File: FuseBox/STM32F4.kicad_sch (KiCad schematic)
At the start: 25 parts, among them J1 61301611121, J2 61301611121, J3 61301611121, J4 61301611121, J5 61301611121, U1 STM32F407VGTx

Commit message: some foo
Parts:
- added C4: 10p, symbol Device:C
- added X1: CG048748M, Custom:CG048748M, symbol Custom:CG048748M
- renumbered C1 to C?, C8 to C?, C9 to C?, C15 to C?, C2 to C?, C11 to C?, C12 to C?, C6 to C?, C14 to C?, C10 to C?, C3 to C?, C5 to C?, C13 to C?, C4 to C?, C7 to C?, FB1 to FB?, J4 to J?, J2 to J?, J3 to J?, J1 to J?, J5 to J?, R1 to R?, R2 to R?, R3 to R?, U1 to U3
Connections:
- net GND: now also C?.2, R?.1, C4.1; no longer R?.2
- net at U3.12 (PH0): now also C?.2, X1.1
- net at U3.13 (PH1): now also C4.2, X1.2
- net at R?.2, U3.14 (NRST): now also C?.1; no longer C?.2
- net at U3.94 (BOOT0): now also R?.2; no longer R?.1
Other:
- moved on the sheet: C15, C?, FB?, J?, R?, U3

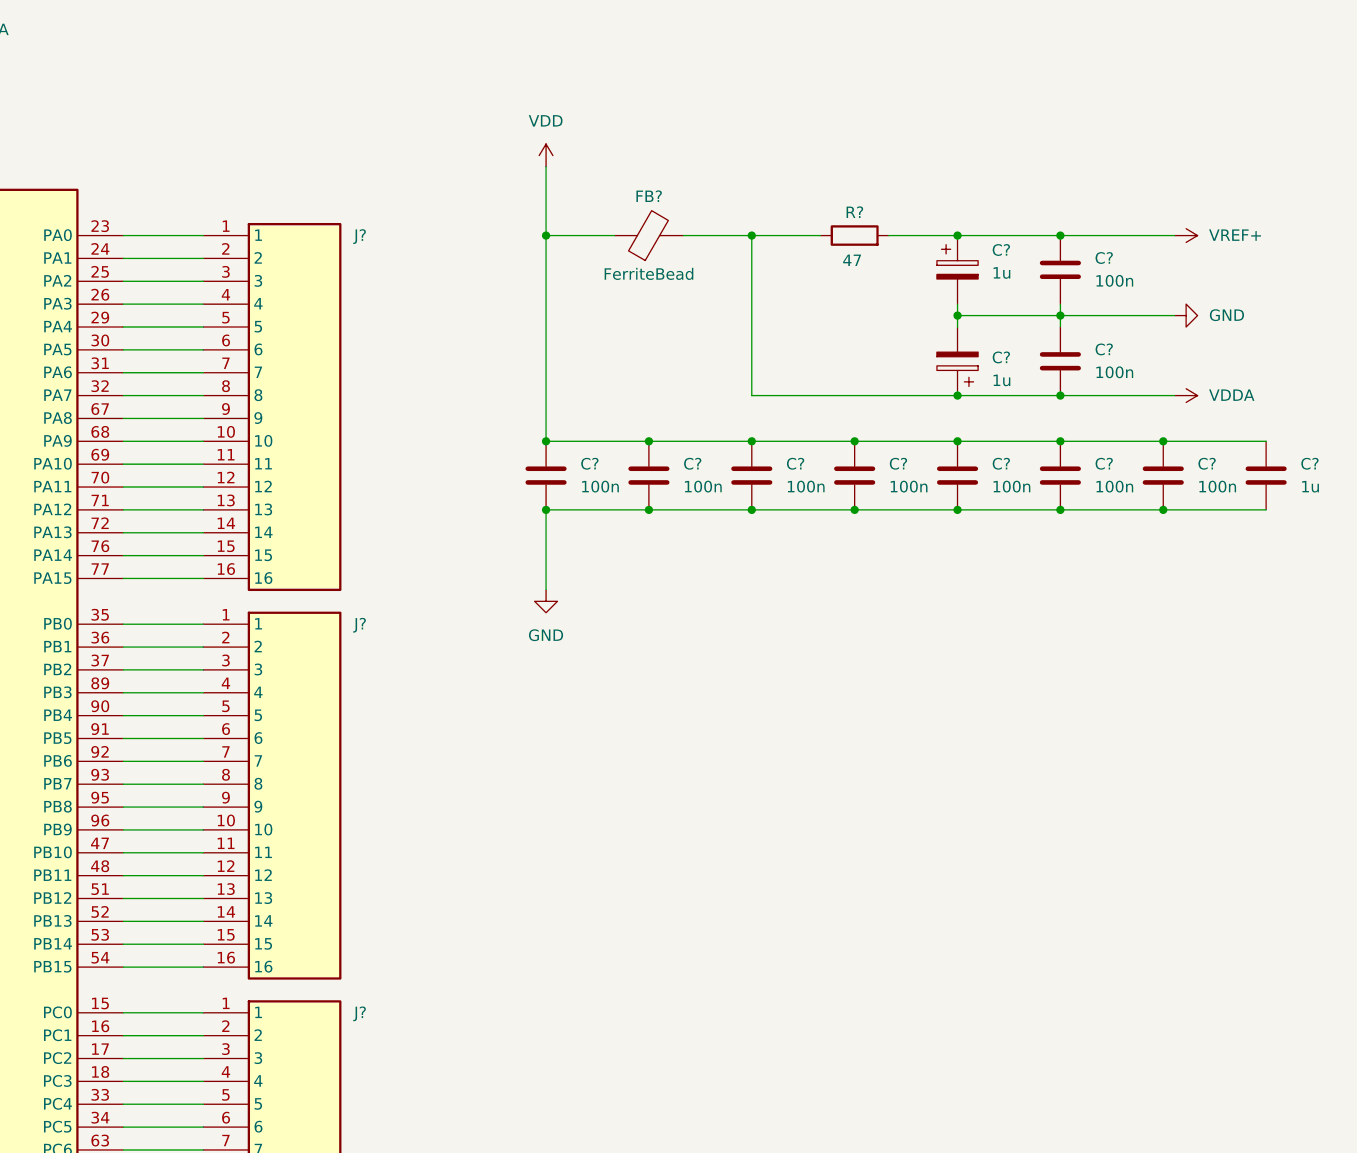
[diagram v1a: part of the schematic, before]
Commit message: added ICE40HX
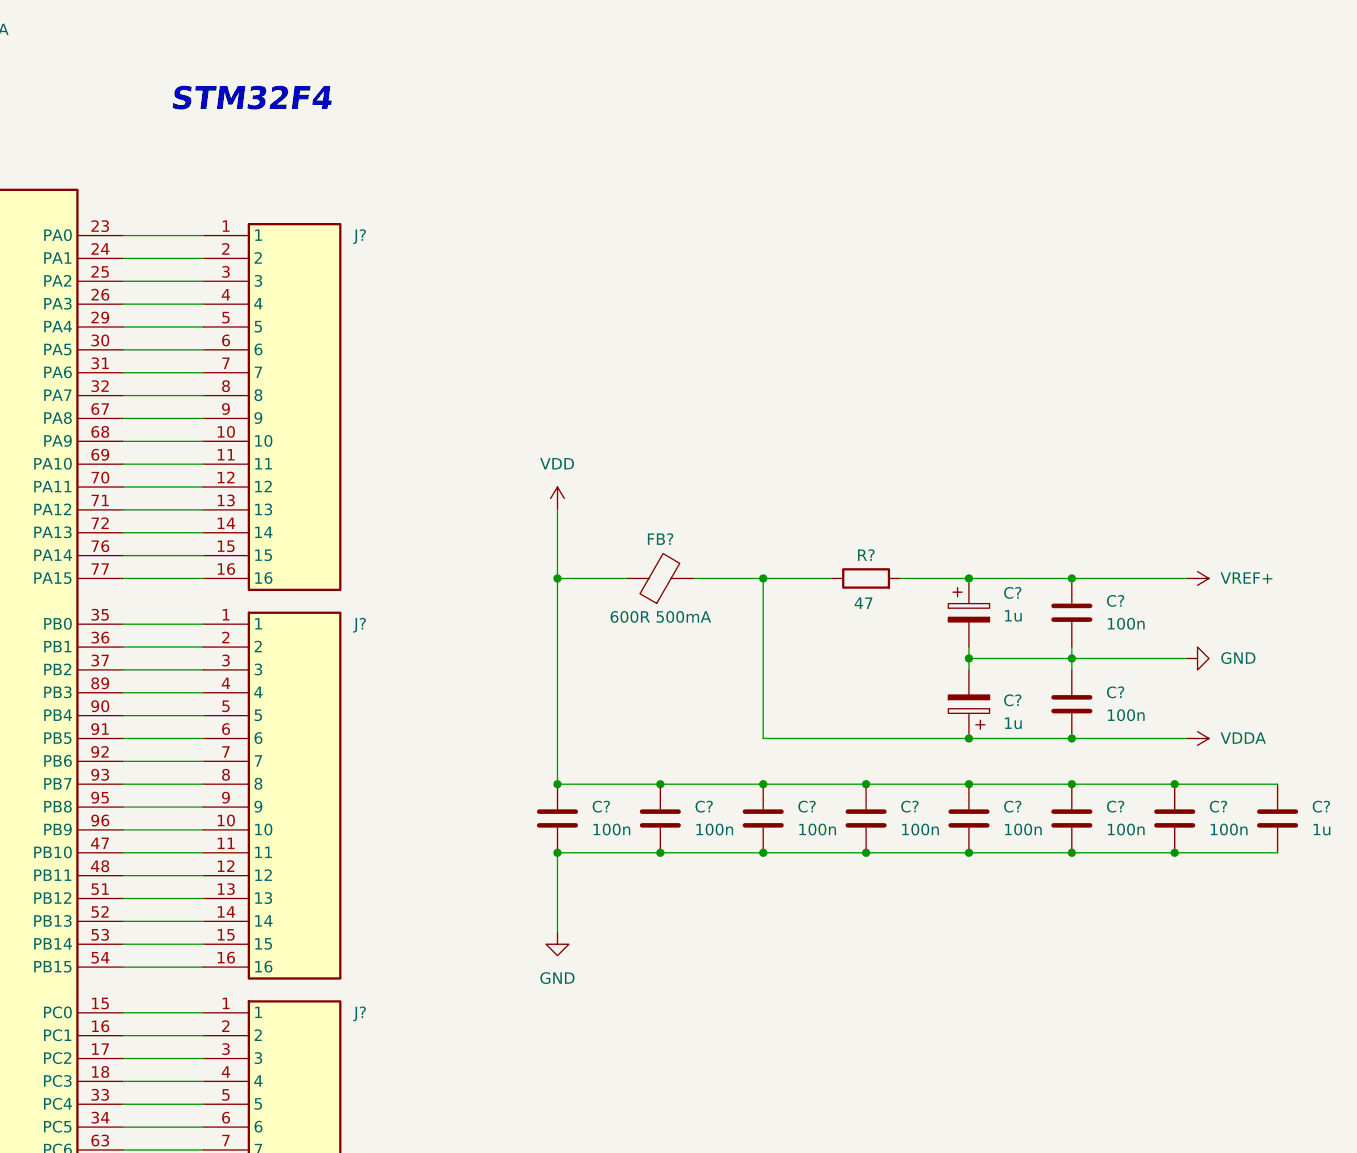
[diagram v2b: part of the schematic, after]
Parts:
- added C?: 100n, symbol Device:C
- C15: renamed from C?; value 100n -> 10p
- FB?: value FerriteBead -> 600R 500mA
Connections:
- net GND: now also C?.2; no longer C15.2
- net at R?.2, U3.14 (NRST): now also C?.1; no longer C15.1
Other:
- note added: "STM32F4"
- moved on the sheet: C?, FB?, R?

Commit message: changes
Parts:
- removed X1: CG048748M, Custom:CG048748M, symbol Custom:CG048748M
- added X1: STDCSU18M, Custom:STDCSU18M, symbol Custom:STDCSU18M
- C15, C4: value 10p -> 20p
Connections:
- net at C15.2, U3.12 (PH0): now also X1.1
- net at C4.2, U3.13 (PH1): now also X1.2
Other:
- note removed: "STM32F4"
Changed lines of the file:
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@@
 	(generator_version "9.0")
 	(paper "A4")
-	(text "STM32F4"
-		(exclude_from_sim no)
-		(at 150.114 26.924 0)
-		(effects
-			(font
-				(size 2.54 2.54)
-				(thickness 0.508)
-				(bold yes)
-				(italic yes)
-			)
-		)
-	)
 	(junction
 		(at 184.15 110.49)
@@
 	)
 	(symbol
-		(lib_id "Custom:CG048748M")
-		(at 30.48 69.85 0)
-		(unit 1)
-		(exclude_from_sim no)
-		(in_bom yes)
-		(on_board yes)
-		(dnp no)
-		(property "Reference" "X1"
-			(at 35.56 65.532 0)
-			(effects
-				(font
-					(size 1.524 1.524)
-				)
-			)
-		)
-		(property "Value" "CG048748M"
-			(at 35.306 74.93 0)
-			(effects
-				(font
-					(size 1.524 1.524)
-				)
-			)
-		)
-		(property "Footprint" "Custom:CG048748M"
-			(at 34.798 78.486 0)
-			(effects
-				(font
-					(size 1.27 1.27)
-					(italic yes)
-				)
-				(hide yes)
-			)
-		)
-		(property "Datasheet" "CG04874-8M"
-			(at 35.052 76.454 0)
-			(effects
-				(font
-					(size 1.27 1.27)
-					(italic yes)
-				)
-				(hide yes)
-			)
-		)
-		(property "Description" ""
-			(at 30.48 69.85 0)
-			(effects
-				(font
-					(size 1.27 1.27)
-				)
-				(hide yes)
-			)
-		)
-		(pin "1"
-		)
-		(pin "2"
-		)
-		(instances
-			(project ""
-				(path "/7cec0856-4a31-46c4-b6e3-cba19fcff38c/e599326e-505d-4a4a-8448-d1c391dfbddc"
-					(reference "X1")
-					(unit 1)
-				)
-			)
-		)
-	)
-	(symbol
 		(lib_id "power:GND")
 		(at 184.15 119.38 0)
@@
 			)
 		)
-		(property "Value" "10p"
+		(property "Value" "20p"
 			(at 29.21 83.8199 0)
 			(effects
@@
 			)
 		)
-		(property "Value" "10p"
+		(property "Value" "20p"
 			(at 49.53 83.8199 0)
 			(effects
@@
 					(unit 1)
 				)
+			)
+		)
+	)
+	(symbol
+		(lib_id "Custom:STDCSU18M")
+		(at 30.48 69.85 0)
+		(unit 1)
+		(exclude_from_sim no)
+		(in_bom yes)
+		(on_board yes)
+		(dnp no)
+		(property "Reference" "X1"
+			(at 35.56 64.77 0)
+			(effects
+				(font
+					(size 1.524 1.524)
+				)
+			)
+		)
+		(property "Value" "STDCSU18M"
+			(at 35.56 74.676 0)
+			(effects
+				(font
+					(size 1.524 1.524)
+				)
+			)
+		)
+		(property "Footprint" "Custom:STDCSU18M"
+			(at 36.068 59.182 0)
+			(effects
+				(font
+					(size 1.27 1.27)
+					(italic yes)
+				)
+				(hide yes)
+			)
+		)
+		(property "Datasheet" "STDCSU1-8M"
+			(at 36.068 61.468 0)
+			(effects
+				(font
+					(size 1.27 1.27)
+					(italic yes)
+				)
+				(hide yes)
+			)
+		)
+		(property "Description" ""
+			(at 30.48 69.85 0)
+			(effects
+				(font
+					(size 1.27 1.27)
+				)
+				(hide yes)
+			)
+		)
+		(pin "2"
+		)
+		(pin "1"
+		)
+		(instances
+			(project ""
+				(path "/7cec0856-4a31-46c4-b6e3-cba19fcff38c/e599326e-505d-4a4a-8448-d1c391dfbddc"
+					(reference "X1")
+					(unit 1)
+				)

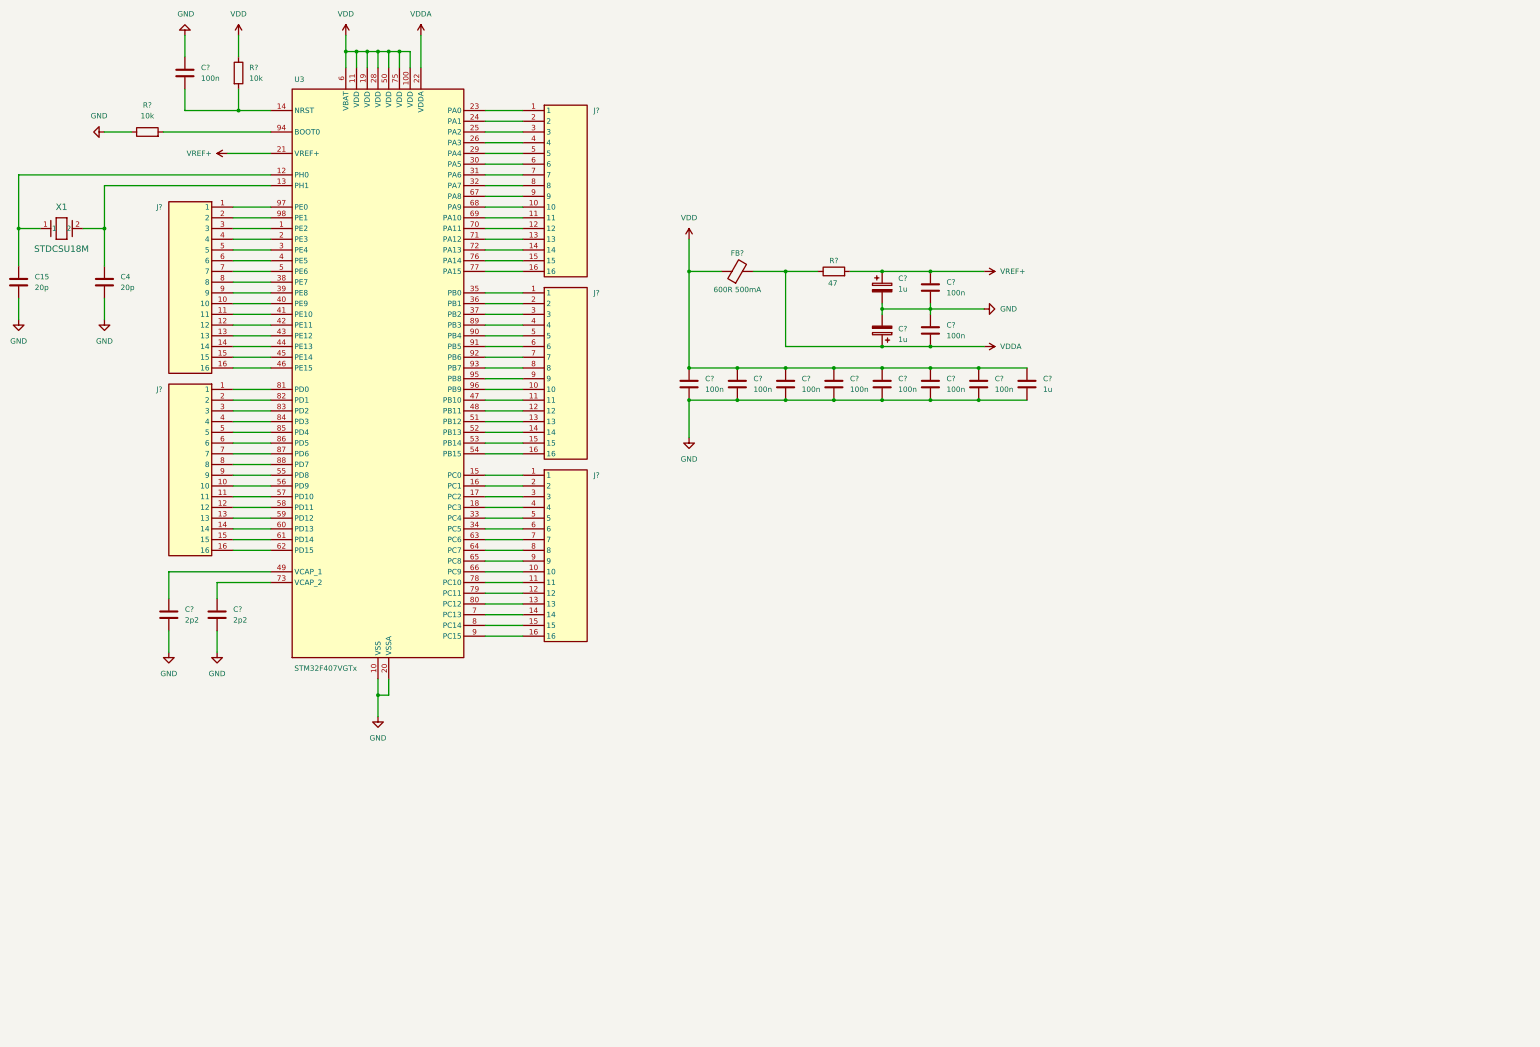
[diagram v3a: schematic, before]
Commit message: added molex terminals
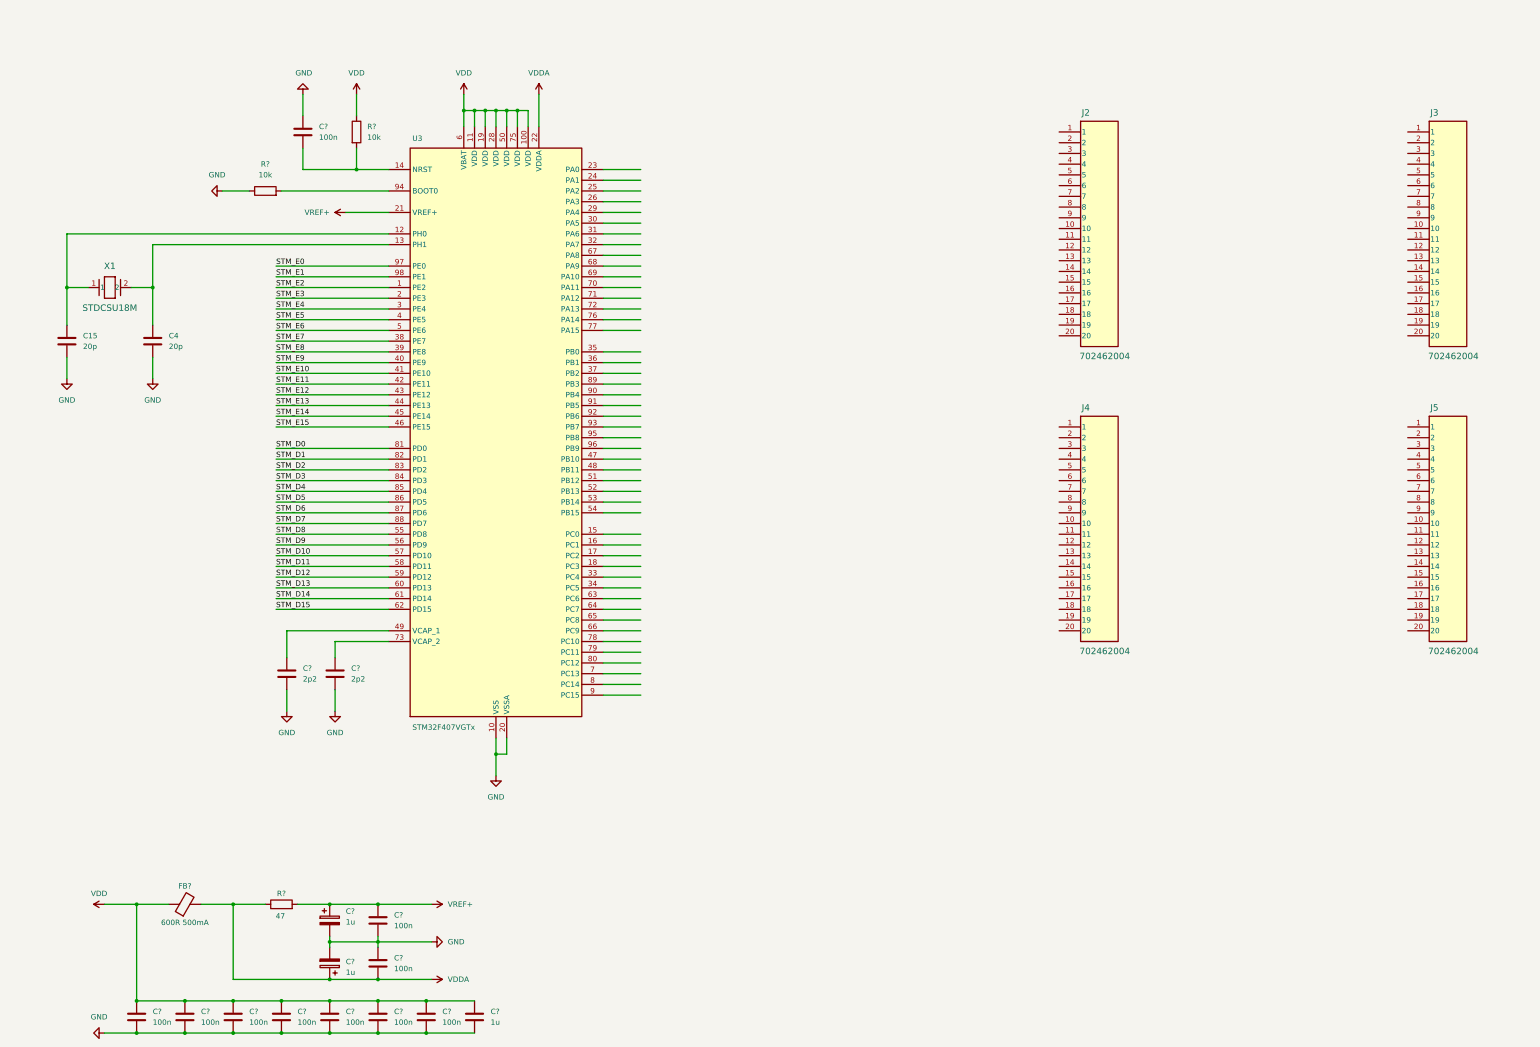
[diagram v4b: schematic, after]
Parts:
- removed J? (x5): 61301611121, Custom:61301611121, symbol Custom:61301611121
- added J2, J3, J4, J5: 702462004, Custom:702462004, symbol Custom:702462004
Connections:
- net STM_E0: now reaches U3.97 (PE0)
- net STM_E9: now reaches U3.40 (PE9)
- net STM_E10: now reaches U3.41 (PE10)
- net STM_E11: now reaches U3.42 (PE11)
- net STM_E12: now reaches U3.43 (PE12)
- net STM_E13: now reaches U3.44 (PE13)
- net STM_E14: now reaches U3.45 (PE14)
- net STM_E15: now reaches U3.46 (PE15)
- net STM_E1: now reaches U3.98 (PE1)
- net STM_E2: now reaches U3.1 (PE2)
- net STM_E3: now reaches U3.2 (PE3)
- net STM_E4: now reaches U3.3 (PE4)
- net STM_E5: now reaches U3.4 (PE5)
- net STM_E6: now reaches U3.5 (PE6)
- net STM_E7: now reaches U3.38 (PE7)
- net STM_E8: now reaches U3.39 (PE8)
- net STM_D8: now reaches U3.55 (PD8)
- net STM_D9: now reaches U3.56 (PD9)
- net STM_D10: now reaches U3.57 (PD10)
- net STM_D11: now reaches U3.58 (PD11)
- net STM_D12: now reaches U3.59 (PD12)
- net STM_D13: now reaches U3.60 (PD13)
- net STM_D14: now reaches U3.61 (PD14)
- net STM_D15: now reaches U3.62 (PD15)
- net STM_D0: now reaches U3.81 (PD0)
- net STM_D1: now reaches U3.82 (PD1)
- net STM_D2: now reaches U3.83 (PD2)
- net STM_D3: now reaches U3.84 (PD3)
- net STM_D4: now reaches U3.85 (PD4)
- net STM_D5: now reaches U3.86 (PD5)
- net STM_D6: now reaches U3.87 (PD6)
- net STM_D7: now reaches U3.88 (PD7)
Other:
- moved on the sheet: C15, C4, C?, FB?, R?, U3, X1
